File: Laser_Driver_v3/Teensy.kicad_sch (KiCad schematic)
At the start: 2 parts, among them U37 CR2013-MI2120

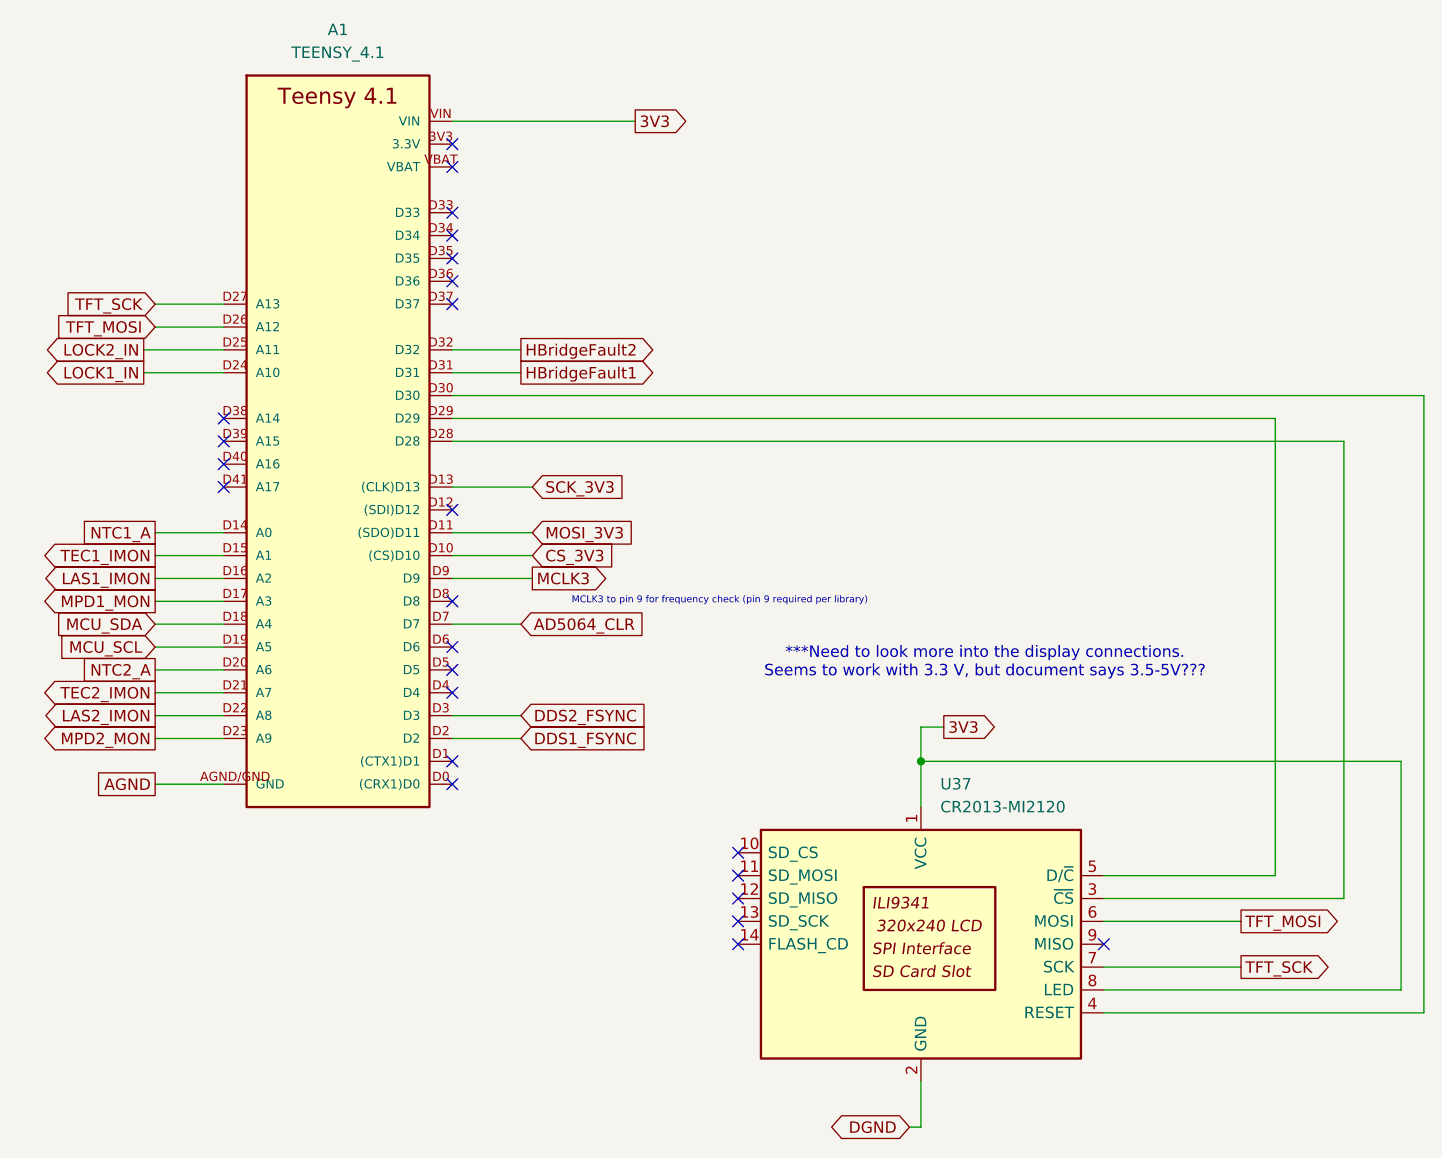
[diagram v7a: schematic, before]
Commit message: Changed to an RF modulation
Based on the uncertainty calculation, needed to change from a low frequency modulation to an RF modulation.  This drive down the noise, but required a very different implentation.  The modulation is limited to about 2 MHz.  Much faster is at the limit of this hardware and would require significant increase in complexity and cost.
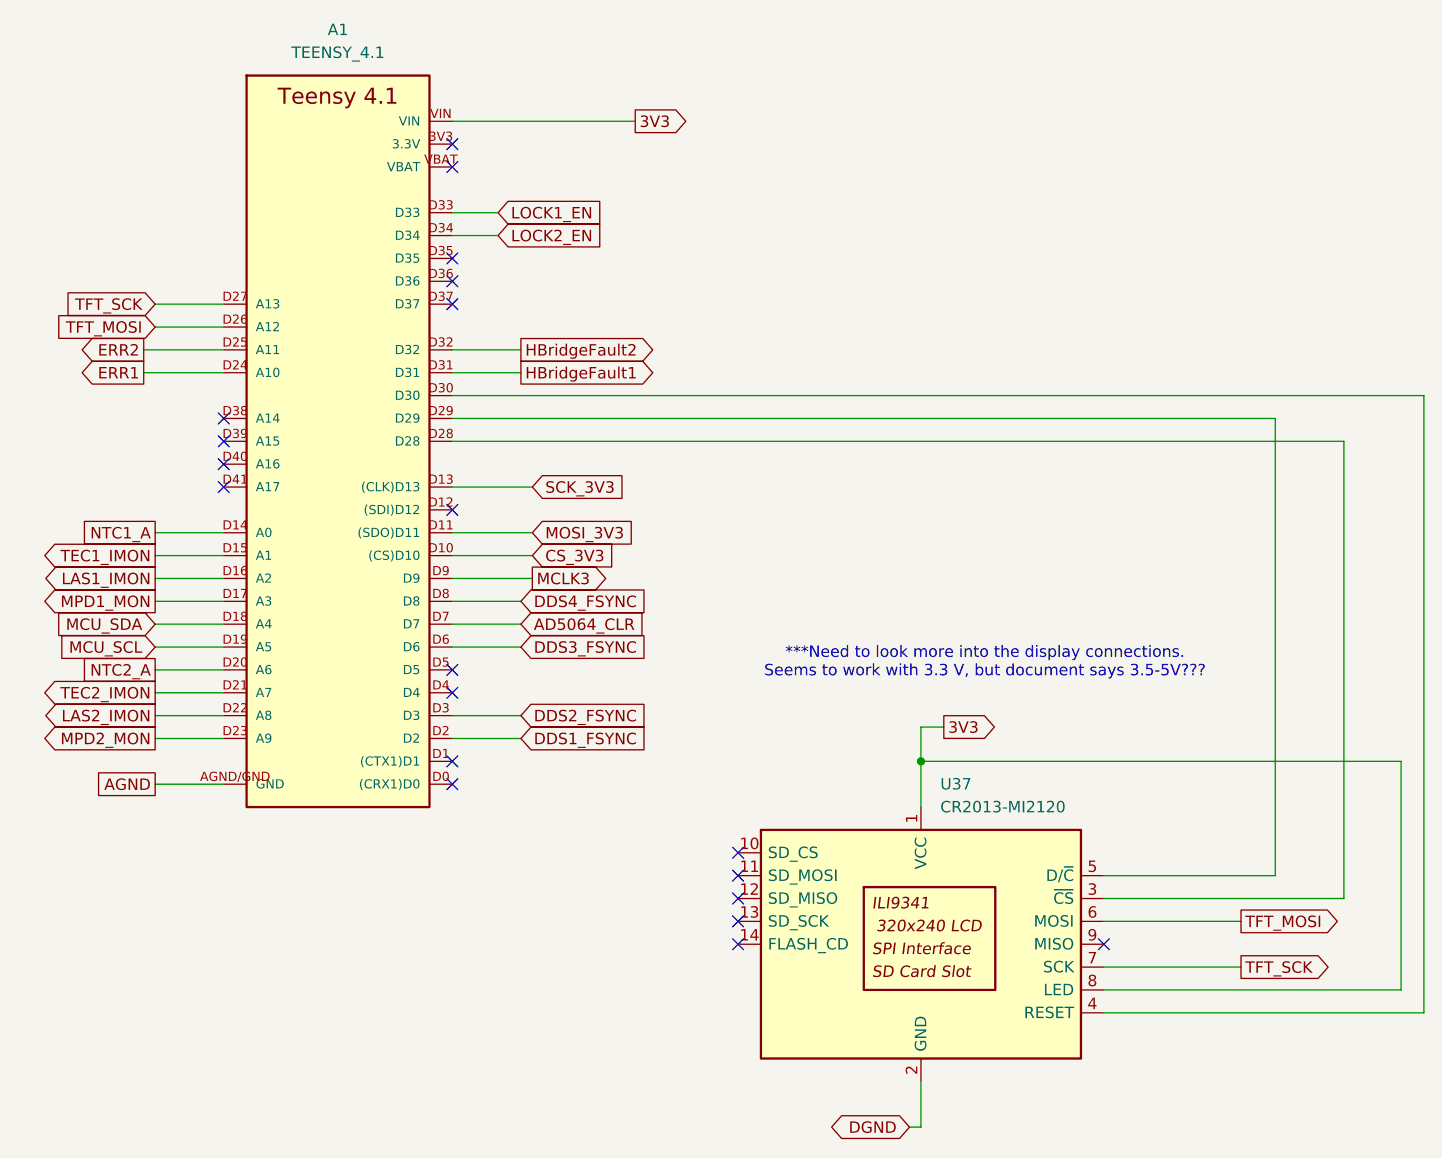
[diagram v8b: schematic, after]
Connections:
- net LOCK1_EN: now reaches A1.D33
- net LOCK2_EN: now reaches A1.D34
- net DDS3_FSYNC: now reaches A1.D6
- net DDS4_FSYNC: now reaches A1.D8
- net LOCK1_IN renamed ERR1
- net LOCK2_IN renamed ERR2
- no-connect marks 24 -> 20
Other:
- note removed: "MCLK3 to pin 9 for frequency check (pin 9 required per library)"
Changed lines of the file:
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@@
 		)
 	)
-	(text "MCLK3 to pin 9 for frequency check (pin 9 required per library)"
-		(exclude_from_sim no)
-		(at 107.188 87.63 0)
-		(effects
-			(font
-				(size 0.762 0.762)
-			)
-		)
-	)
 	(junction
 		(at 129.54 105.41)
@@
 	)
 	(no_connect
-		(at 77.47 87.63)
-	)
-	(no_connect
-		(at 77.47 44.45)
-	)
-	(no_connect
-		(at 77.47 92.71)
-	)
-	(no_connect
 		(at 109.22 120.65)
 	)
@@
 	)
 	(no_connect
-		(at 77.47 46.99)
-	)
-	(no_connect
 		(at 149.86 125.73)
 	)
@@
 	(wire
 		(pts
+			(xy 77.47 46.99) (xy 82.55 46.99)
+		)
+		(stroke
+			(width 0)
+			(type default)
+		)
+	)
+	(wire
+		(pts
 			(xy 149.86 130.81) (xy 182.88 130.81)
 		)
@@
 	(wire
 		(pts
+			(xy 77.47 87.63) (xy 85.09 87.63)
+		)
+		(stroke
+			(width 0)
+			(type default)
+		)
+	)
+	(wire
+		(pts
 			(xy 129.54 101.6) (xy 129.54 105.41)
 		)
@@
 	(wire
 		(pts
+			(xy 77.47 92.71) (xy 85.09 92.71)
+		)
+		(stroke
+			(width 0)
+			(type default)
+		)
+	)
+	(wire
+		(pts
 			(xy 44.45 92.71) (xy 52.07 92.71)
 		)
@@
 	(wire
 		(pts
+			(xy 77.47 44.45) (xy 82.55 44.45)
+		)
+		(stroke
+			(width 0)
+			(type default)
+		)
+	)
+	(wire
+		(pts
 			(xy 43.18 59.69) (xy 52.07 59.69)
 		)
@@
 		)
 	)
-	(global_label "LOCK2_IN"
+	(global_label "ERR2"
 		(shape output)
 		(at 43.18 59.69 180)
@@
 		)
 		(property "Intersheetrefs" "${INTERSHEET_REFS}"
-			(at 31.1838 59.69 0)
+			(at 35.2963 59.69 0)
 			(hide yes)
 			(show_name no)
@@
 		)
 	)
+	(global_label "DDS3_FSYNC"
+		(shape input)
+		(at 85.09 92.71 0)
+		(fields_autoplaced yes)
+		(effects
+			(font
+				(size 1.27 1.27)
+			)
+			(justify left)
+		)
+		(property "Intersheetrefs" "${INTERSHEET_REFS}"
+			(at 99.989 92.71 0)
+			(hide yes)
+			(show_name no)
+			(do_not_autoplace no)
+			(effects
+				(font
+					(size 1.27 1.27)
+				)
+				(justify left)
+			)
+		)
+	)
 	(global_label "NTC2_A"
 		(shape passive)
@@
 		)
 	)
+	(global_label "LOCK2_EN"
+		(shape input)
+		(at 82.55 46.99 0)
+		(fields_autoplaced yes)
+		(effects
+			(font
+				(size 1.27 1.27)
+			)
+			(justify left)
+		)
+		(property "Intersheetrefs" "${INTERSHEET_REFS}"
+			(at 95.0904 46.99 0)
+			(hide yes)
+			(show_name no)
+			(do_not_autoplace no)
+			(effects
+				(font
+					(size 1.27 1.27)
+				)
+				(justify left)
+			)
+		)
+	)
+	(global_label "DDS4_FSYNC"
+		(shape input)
+		(at 85.09 87.63 0)
+		(fields_autoplaced yes)
+		(effects
+			(font
+				(size 1.27 1.27)
+			)
+			(justify left)
+		)
+		(property "Intersheetrefs" "${INTERSHEET_REFS}"
+			(at 99.989 87.63 0)
+			(hide yes)
+			(show_name no)
+			(do_not_autoplace no)
+			(effects
+				(font
+					(size 1.27 1.27)
+				)
+				(justify left)
+			)
+		)
+	)
 	(global_label "MCLK3"
 		(shape output)
@@
 		)
 	)
-	(global_label "LOCK1_IN"
+	(global_label "ERR1"
 		(shape output)
 		(at 43.18 62.23 180)
@@
 		)
 		(property "Intersheetrefs" "${INTERSHEET_REFS}"
-			(at 31.1838 62.23 0)
+			(at 35.2963 62.23 0)
 			(hide yes)
 			(show_name no)
@@
 			(hide yes)
 			(show_name no)
+			(do_not_autoplace no)
+			(effects
+				(font
+					(size 1.27 1.27)
+				)
+				(justify left)
+			)
+		)
+	)
+	(global_label "LOCK1_EN"
+		(shape input)
+		(at 82.55 44.45 0)
+		(fields_autoplaced yes)
+		(effects
+			(font
+				(size 1.27 1.27)
+			)
+			(justify left)
+		)
+		(property "Intersheetrefs" "${INTERSHEET_REFS}"
+			(at 95.0904 44.45 0)
+			(hide yes)
+			(show_name no)
